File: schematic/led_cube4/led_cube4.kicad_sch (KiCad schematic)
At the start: 17 parts, among them J2 Conn_01x08_Pin, SW1 SW_Push, SW2 SW_Push, SW3 SW_Push, U1 L7805, U2 ATmega16A-P, Y1 14.7456MHz

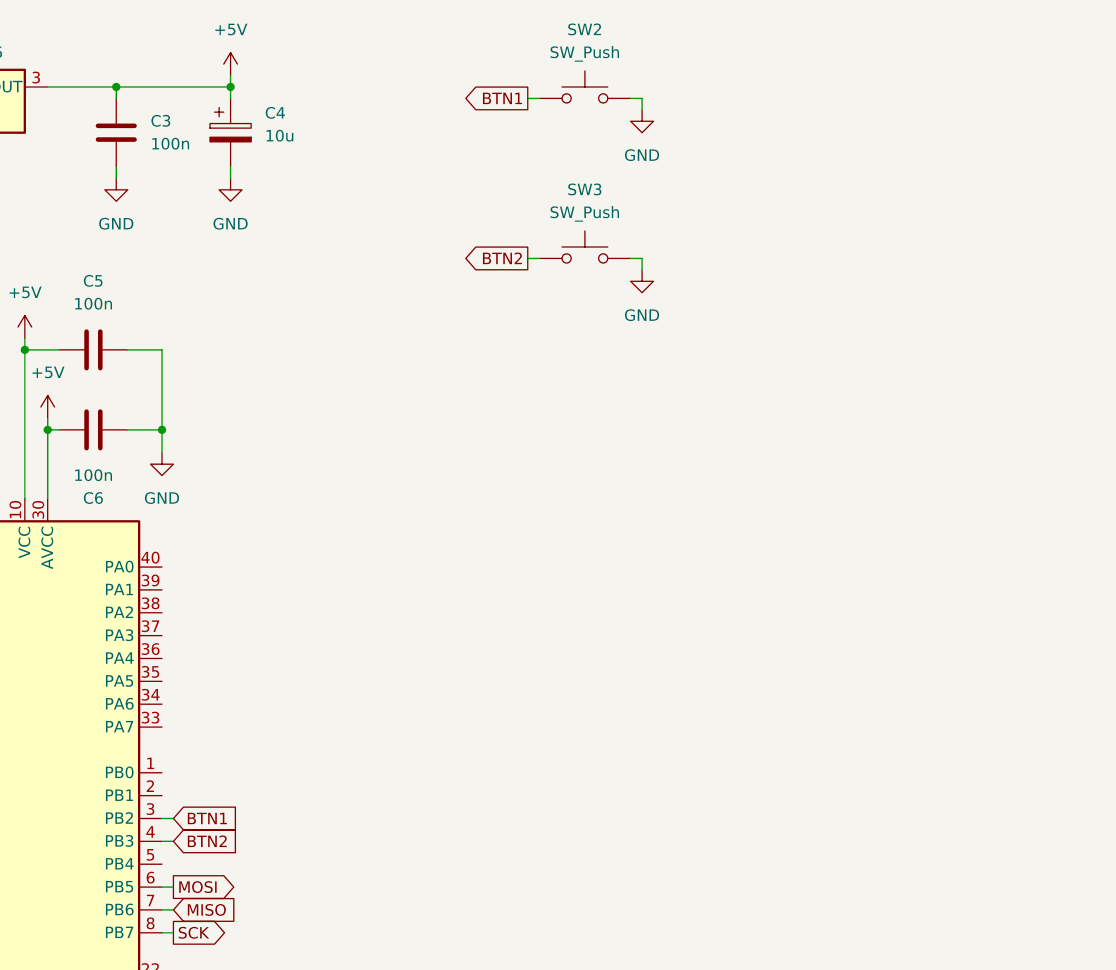
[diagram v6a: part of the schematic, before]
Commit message: feat(schematic): add signal LEDs
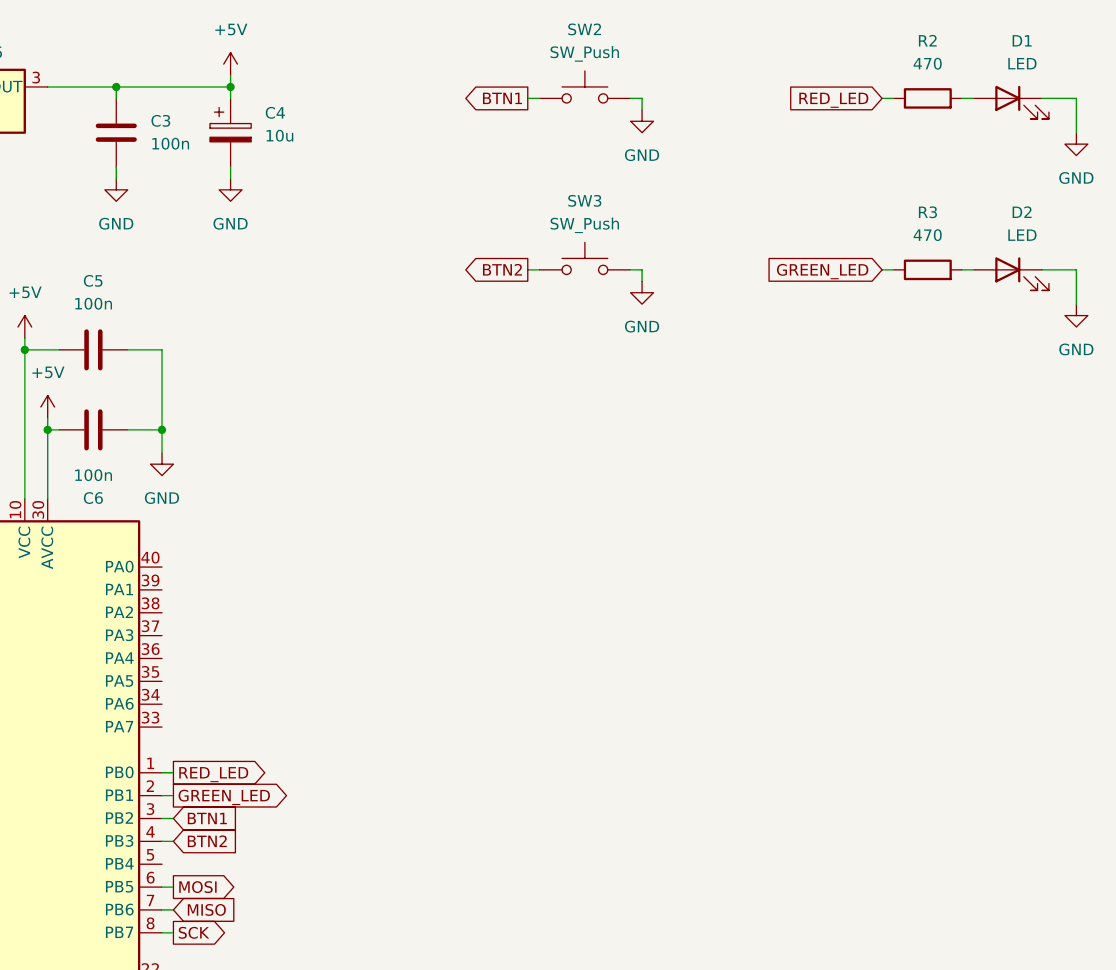
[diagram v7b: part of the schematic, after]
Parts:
- added D1, D2: LED, symbol Device:LED
- added R2, R3: 470, symbol Device:R
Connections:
- net GND: now also D1.1 (K), D2.1 (K)
- net RED_LED: now reaches U2.1 (PB0)
- net RED_LED: now also R2.1
- net GREEN_LED: now reaches U2.2 (PB1)
- net GREEN_LED: now also R3.1
- new net: D2.2 (A), R3.2
- new net: D1.2 (A), R2.2
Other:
- moved on the sheet: SW3

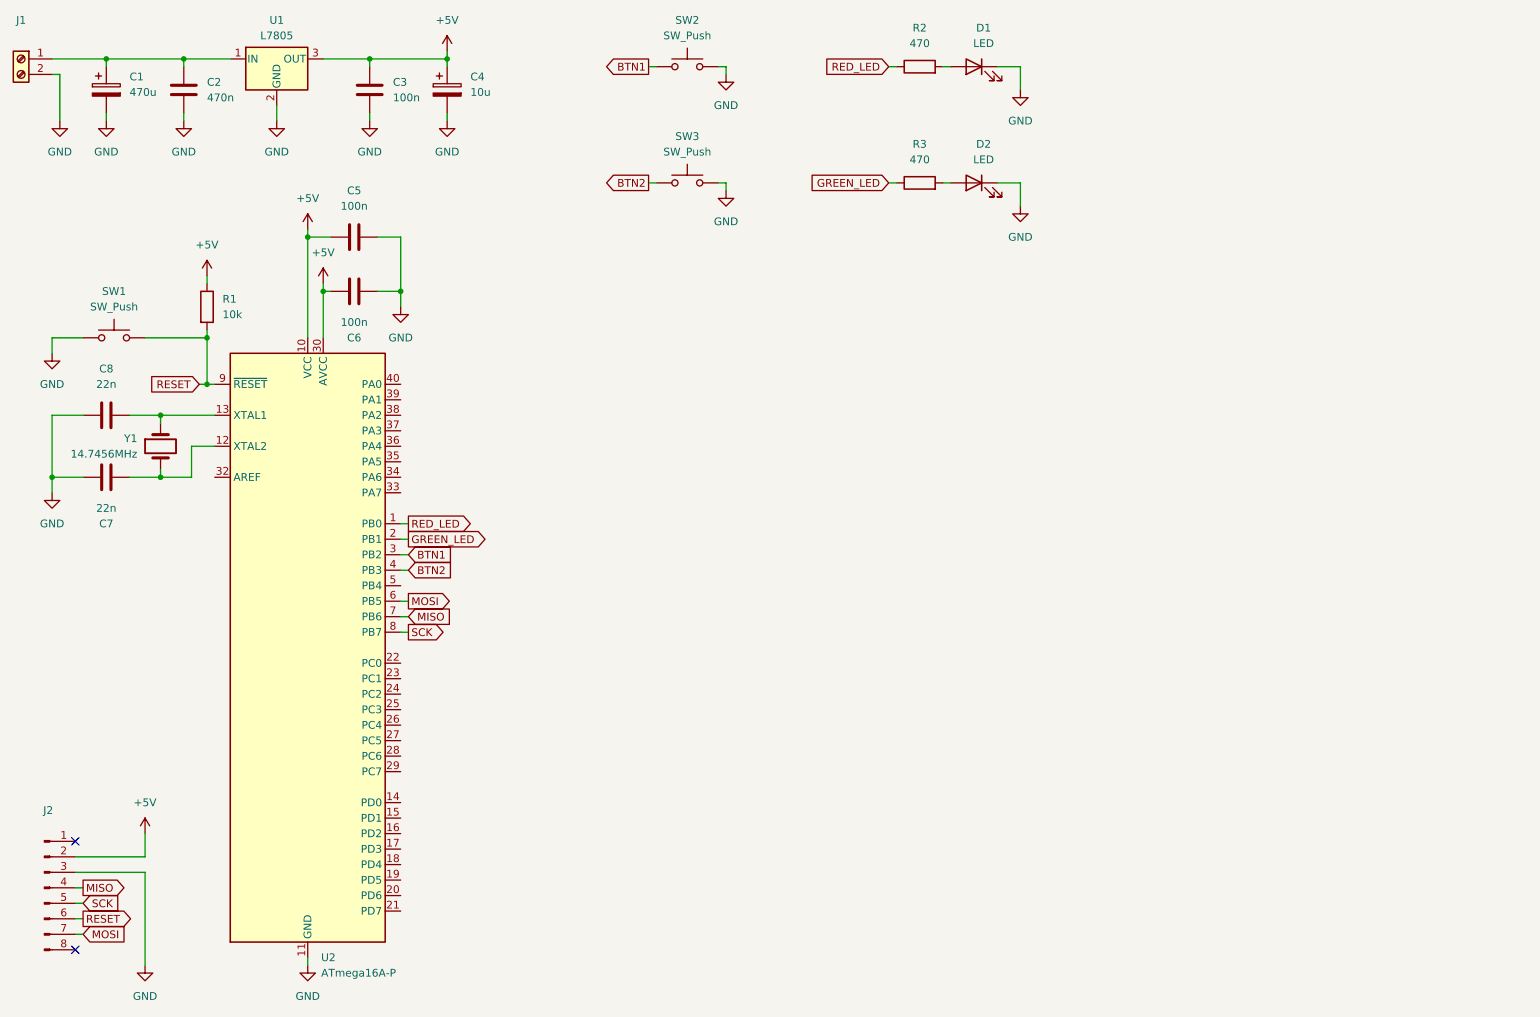
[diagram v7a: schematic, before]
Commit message: feat(schematic): add LEDs control circuit
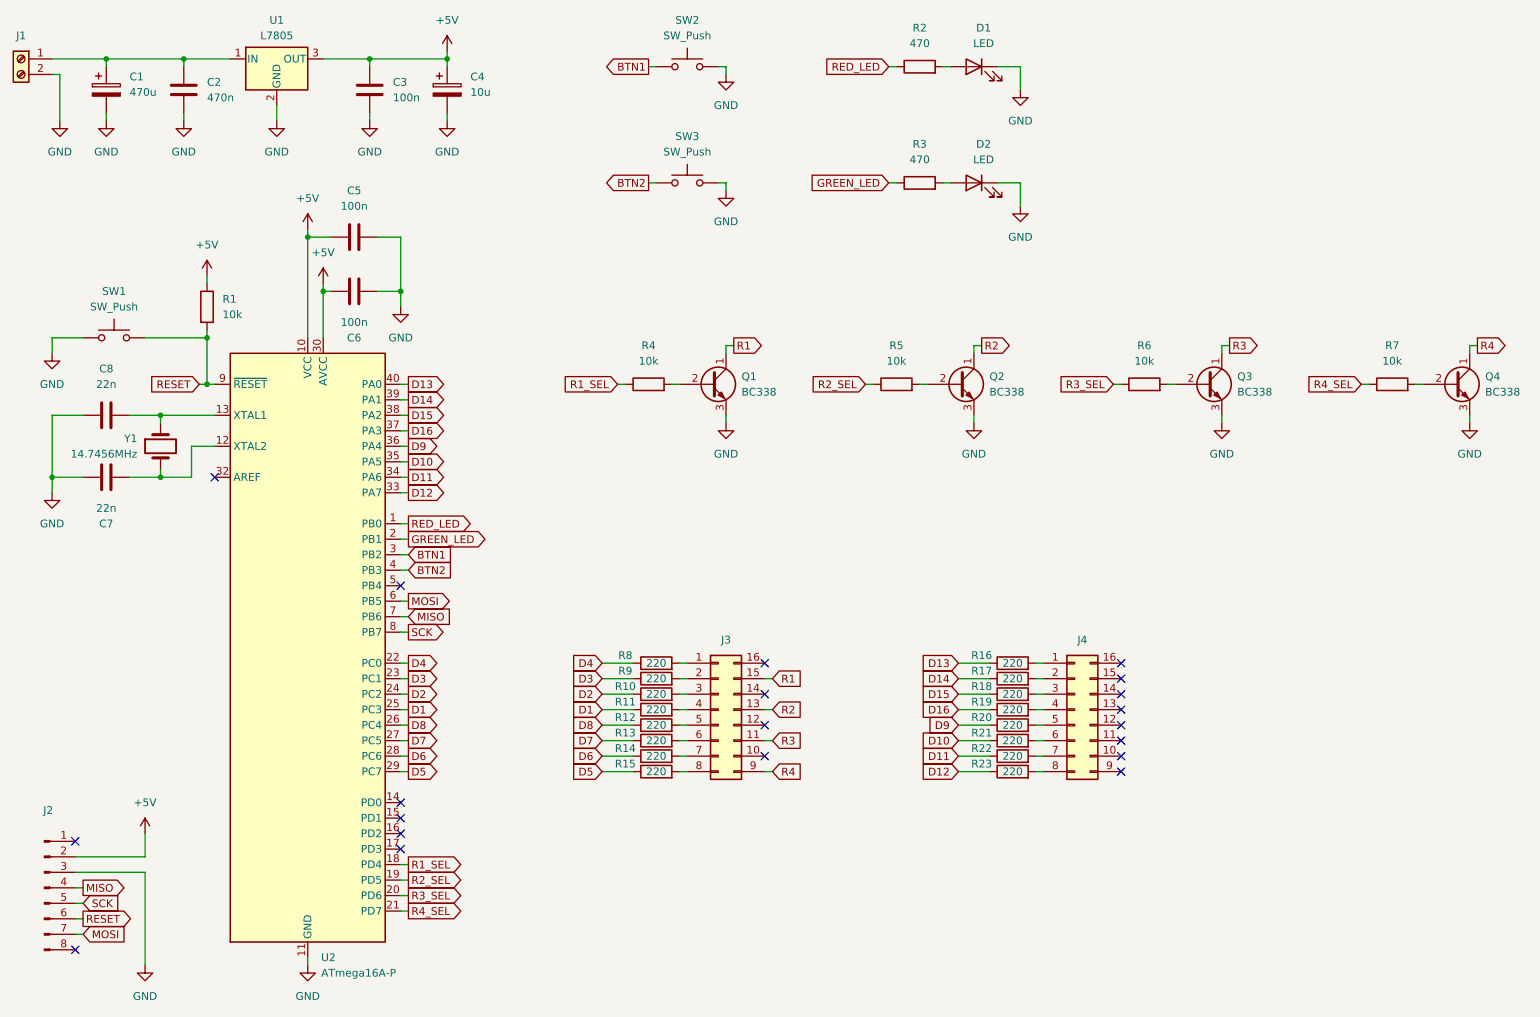
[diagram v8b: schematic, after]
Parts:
- added J3, J4: Conn_02x08_Counter_Clockwise, symbol Connector_Generic:Conn_02x08_Counter_Clockwise
- added Q1, Q2, Q3, Q4: BC338, Package_TO_SOT_THT:TO-92_Inline, symbol Transistor_BJT:BC338
- added R10, R11, R12, R13, R14, R15, R16, R17, R18, R19, R20, R21, R22, R23, R8, R9: 220, symbol Device:R
- added R4, R5, R6, R7: 10k, symbol Device:R
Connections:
- net GND: now also Q1.3 (E), Q2.3 (E), Q3.3 (E), Q4.3 (E)
- net R1_SEL: now reaches U2.18 (PD4)
- net R1_SEL: now also R4.1
- net R2_SEL: now reaches U2.19 (PD5)
- net R2_SEL: now also R5.1
- net R3_SEL: now reaches U2.20 (PD6)
- net R3_SEL: now also R6.1
- net R4_SEL: now reaches U2.21 (PD7)
- net R4_SEL: now also R7.1
- net D4: now reaches U2.22 (PC0)
- net D4: now also R8.1
- net D3: now reaches U2.23 (PC1)
- net D3: now also R9.1
- net D2: now reaches U2.24 (PC2)
- net D2: now also R10.1
- net D1: now reaches U2.25 (PC3)
- net D1: now also R11.1
- net D8: now reaches U2.26 (PC4)
- net D8: now also R12.1
- net D7: now reaches U2.27 (PC5)
- net D7: now also R13.1
- net D6: now reaches U2.28 (PC6)
- net D6: now also R14.1
- net D5: now reaches U2.29 (PC7)
- net D5: now also R15.1
- net D12: now reaches U2.33 (PA7)
- net D12: now also R23.1
- net D11: now reaches U2.34 (PA6)
- net D11: now also R22.1
- net D10: now reaches U2.35 (PA5)
- net D10: now also R21.1
- net D9: now reaches U2.36 (PA4)
- net D9: now also R20.1
- net D16: now reaches U2.37 (PA3)
- net D16: now also R19.1
- net D15: now reaches U2.38 (PA2)
- net D15: now also R18.1
- net D14: now reaches U2.39 (PA1)
- net D14: now also R17.1
- net D13: now reaches U2.40 (PA0)
- net D13: now also R16.1
- new net: J3.6 (Pin_6), R13.2
- new net: J4.3 (Pin_3), R18.2
- new net: J3.1 (Pin_1), R8.2
- new net: J3.2 (Pin_2), R9.2
- new net: J3.3 (Pin_3), R10.2
- new net: J3.4 (Pin_4), R11.2
- new net: J3.5 (Pin_5), R12.2
- new net: J3.7 (Pin_7), R14.2
- new net: J3.8 (Pin_8), R15.2
- new net: J4.1 (Pin_1), R16.2
- new net: J4.2 (Pin_2), R17.2
- new net: J4.4 (Pin_4), R19.2
- new net: J4.5 (Pin_5), R20.2
- new net: J4.6 (Pin_6), R21.2
- new net: J4.7 (Pin_7), R22.2
- new net: J4.8 (Pin_8), R23.2
- new net: Q3.2 (B), R6.2
- new net: Q1.2 (B), R4.2
- new net: Q2.2 (B), R5.2
- new net: Q4.2 (B), R7.2
- new net R1: J3.15 (Pin_15), Q1.1 (C)
- new net R2: J3.13 (Pin_13), Q2.1 (C)
- new net R3: J3.11 (Pin_11), Q3.1 (C)
- new net R4: J3.9 (Pin_9), Q4.1 (C)
- no-connect marks 2 -> 20
